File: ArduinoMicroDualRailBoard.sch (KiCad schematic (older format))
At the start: 54 parts, among them J1 Conn_01x20_Male, J2 Screw_Terminal_01x03, J3 Conn_01x20_Male, J4 Conn_01x20_Male, J5 Screw_Terminal_01x03, J6 Conn_01x20_Male, J7 SDS-50J, J8 SDS-50J, U1 L7805, U2 L7815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

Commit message: PCB layout #2
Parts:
- added J9: Screw_Terminal_01x03, TerminalBlock:TerminalBlock_bornier-3_P5.08mm, symbol Connector:Screw_Terminal_01x03
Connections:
- net +15V: now also J9.3 (Pin_3)
- net -15V: now also J9.1 (Pin_1)
- net GND: now also J9.2 (Pin_2)
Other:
- moved on the sheet: J5
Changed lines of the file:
@@
 L Connector:Screw_Terminal_01x03 J5
 U 1 1 60BD4254
-P 3050 6100
-F 0 "J5" H 3000 5850 50  0000 L CNN
-F 1 "Screw_Terminal_01x03" V 3150 5700 50  0000 L CNN
-F 2 "TerminalBlock:TerminalBlock_bornier-3_P5.08mm" H 3050 6100 50  0001 C CNN
-F 3 "~" H 3050 6100 50  0001 C CNN
-	1    3050 6100
+P 3050 5750
+F 0 "J5" H 3000 5500 50  0000 L CNN
+F 1 "Screw_Terminal_01x03" V 3150 5350 50  0000 L CNN
+F 2 "TerminalBlock:TerminalBlock_bornier-3_P5.08mm" H 3050 5750 50  0001 C CNN
+F 3 "~" H 3050 5750 50  0001 C CNN
+	1    3050 5750
 	-1   0    0    1
 $EndComp
@@
 L power:+15V #PWR0131
 U 1 1 60C5B353
-P 3350 5900
-F 0 "#PWR0131" H 3350 5750 50  0001 C CNN
-F 1 "+15V" H 3365 6073 50  0000 C CNN
-F 2 "" H 3350 5900 50  0001 C CNN
-F 3 "" H 3350 5900 50  0001 C CNN
-	1    3350 5900
+P 3350 5550
+F 0 "#PWR0131" H 3350 5400 50  0001 C CNN
+F 1 "+15V" H 3365 5723 50  0000 C CNN
+F 2 "" H 3350 5550 50  0001 C CNN
+F 3 "" H 3350 5550 50  0001 C CNN
+	1    3350 5550
 	1    0    0    -1
 $EndComp
@@
 L power:GND #PWR0132
 U 1 1 60C5D4D3
-P 3550 6300
-F 0 "#PWR0132" H 3550 6050 50  0001 C CNN
-F 1 "GND" H 3555 6127 50  0000 C CNN
-F 2 "" H 3550 6300 50  0001 C CNN
-F 3 "" H 3550 6300 50  0001 C CNN
-	1    3550 6300
+P 3550 5950
+F 0 "#PWR0132" H 3550 5700 50  0001 C CNN
+F 1 "GND" H 3555 5777 50  0000 C CNN
+F 2 "" H 3550 5950 50  0001 C CNN
+F 3 "" H 3550 5950 50  0001 C CNN
+	1    3550 5950
 	1    0    0    -1
 $EndComp
@@
 L power:-15V #PWR0133
 U 1 1 60C5DC2B
-P 3350 6300
-F 0 "#PWR0133" H 3350 6400 50  0001 C CNN
-F 1 "-15V" H 3365 6473 50  0000 C CNN
-F 2 "" H 3350 6300 50  0001 C CNN
-F 3 "" H 3350 6300 50  0001 C CNN
-	1    3350 6300
-	-1   0    0    1
-$EndComp
-Wire Wire Line
-	3250 6200 3350 6200
-Wire Wire Line
-	3350 6200 3350 6300
-Wire Wire Line
-	3250 6100 3550 6100
-Wire Wire Line
-	3550 6100 3550 6300
-Wire Wire Line
-	3250 6000 3350 6000
-Wire Wire Line
-	3350 6000 3350 5900
+P 3350 5950
+F 0 "#PWR0133" H 3350 6050 50  0001 C CNN
+F 1 "-15V" H 3365 6123 50  0000 C CNN
+F 2 "" H 3350 5950 50  0001 C CNN
+F 3 "" H 3350 5950 50  0001 C CNN
+	1    3350 5950
+	-1   0    0    1
+$EndComp
+Wire Wire Line
+	3250 5850 3350 5850
+Wire Wire Line
+	3350 5850 3350 5950
+Wire Wire Line
+	3250 5750 3550 5750
+Wire Wire Line
+	3550 5750 3550 5950
+Wire Wire Line
+	3250 5650 3350 5650
+Wire Wire Line
+	3350 5650 3350 5550
 NoConn ~ 4200 5800
 NoConn ~ 6750 6400
@@
 Wire Wire Line
 	4100 4300 4200 4300
+$Comp
+L Connector:Screw_Terminal_01x03 J9
+U 1 1 5FC225DB
+P 3050 6700
+F 0 "J9" H 3000 6450 50  0000 L CNN
+F 1 "Screw_Terminal_01x03" V 3150 6300 50  0000 L CNN
+F 2 "TerminalBlock:TerminalBlock_bornier-3_P5.08mm" H 3050 6700 50  0001 C CNN
+F 3 "~" H 3050 6700 50  0001 C CNN
+	1    3050 6700
+	-1   0    0    1
+$EndComp
+$Comp
+L power:+15V #PWR01
+U 1 1 5FC225E1
+P 3350 6500
+F 0 "#PWR01" H 3350 6350 50  0001 C CNN
+F 1 "+15V" H 3365 6673 50  0000 C CNN
+F 2 "" H 3350 6500 50  0001 C CNN
+F 3 "" H 3350 6500 50  0001 C CNN
+	1    3350 6500
+	1    0    0    -1
+$EndComp
+$Comp
+L power:GND #PWR03
+U 1 1 5FC225E7
+P 3550 6900
+F 0 "#PWR03" H 3550 6650 50  0001 C CNN
+F 1 "GND" H 3555 6727 50  0000 C CNN
+F 2 "" H 3550 6900 50  0001 C CNN
+F 3 "" H 3550 6900 50  0001 C CNN
+	1    3550 6900
+	1    0    0    -1
+$EndComp
+$Comp
+L power:-15V #PWR02
+U 1 1 5FC225ED
+P 3350 6900
+F 0 "#PWR02" H 3350 7000 50  0001 C CNN
+F 1 "-15V" H 3365 7073 50  0000 C CNN
+F 2 "" H 3350 6900 50  0001 C CNN
+F 3 "" H 3350 6900 50  0001 C CNN
+	1    3350 6900
+	-1   0    0    1
+$EndComp
+Wire Wire Line
+	3250 6800 3350 6800
+Wire Wire Line
+	3350 6800 3350 6900
+Wire Wire Line
+	3250 6700 3550 6700
+Wire Wire Line
+	3550 6700 3550 6900
+Wire Wire Line
+	3250 6600 3350 6600
+Wire Wire Line
+	3350 6600 3350 6500
 $EndSCHEMATC

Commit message: Finished routing
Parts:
- added J10: Conn_01x02_Male, Connector_PinHeader_2.54mm:PinHeader_1x02_P2.54mm_Vertical, symbol Connector:Conn_01x02_Male
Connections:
- net +5V: now also J10.2 (Pin_2); no longer C14.2, U4.12 (+5V)
- new net: C14.2, J10.1 (Pin_1), U4.12 (+5V)
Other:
- note added: "PLACE JUMPER FOR NORMAL OPERATION\nREMOVE JUMPER WHEN POWERED BY USB"
- note added: "V"
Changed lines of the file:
@@
 L power:+5V #PWR0112
 U 1 1 5FE7786C
-P 6750 6050
-F 0 "#PWR0112" H 6750 5900 50  0001 C CNN
-F 1 "+5V" H 6765 6223 50  0000 C CNN
-F 2 "" H 6750 6050 50  0001 C CNN
-F 3 "" H 6750 6050 50  0001 C CNN
-	1    6750 6050
+P 7100 5500
+F 0 "#PWR0112" H 7100 5350 50  0001 C CNN
+F 1 "+5V" H 7115 5673 50  0000 C CNN
+F 2 "" H 7100 5500 50  0001 C CNN
+F 3 "" H 7100 5500 50  0001 C CNN
+	1    7100 5500
 	1    0    0    -1
 $EndComp
@@
 Wire Wire Line
 	6500 6100 6750 6100
-Wire Wire Line
-	6750 6100 6750 6050
 $Comp
 L Device:C C14
@@
 Wire Wire Line
 	3350 6600 3350 6500
+$Comp
+L Connector:Conn_01x02_Male J10
+U 1 1 5FD0AFC4
+P 7400 5700
+F 0 "J10" H 7372 5582 50  0000 R CNN
+F 1 "Conn_01x02_Male" H 7850 5750 50  0000 R CNN
+F 2 "Connector_PinHeader_2.54mm:PinHeader_1x02_P2.54mm_Vertical" H 7400 5700 50  0001 C CNN
+F 3 "~" H 7400 5700 50  0001 C CNN
+	1    7400 5700
+	-1   0    0    1
+$EndComp
+Wire Wire Line
+	6750 5700 7200 5700
+Wire Wire Line
+	6750 5700 6750 6100
+Wire Wire Line
+	7100 5500 7100 5600
+Wire Wire Line
+	7100 5600 7200 5600
+Text Notes 5950 5200 0    50   ~ 0
+PLACE JUMPER FOR NORMAL OPERATION\nREMOVE JUMPER WHEN POWERED BY USB
+Wire Notes Line
+	7350 5500 7350 5250
+Text Notes 7396 5549 2    100  ~ 0
+V
 $EndSCHEMATC

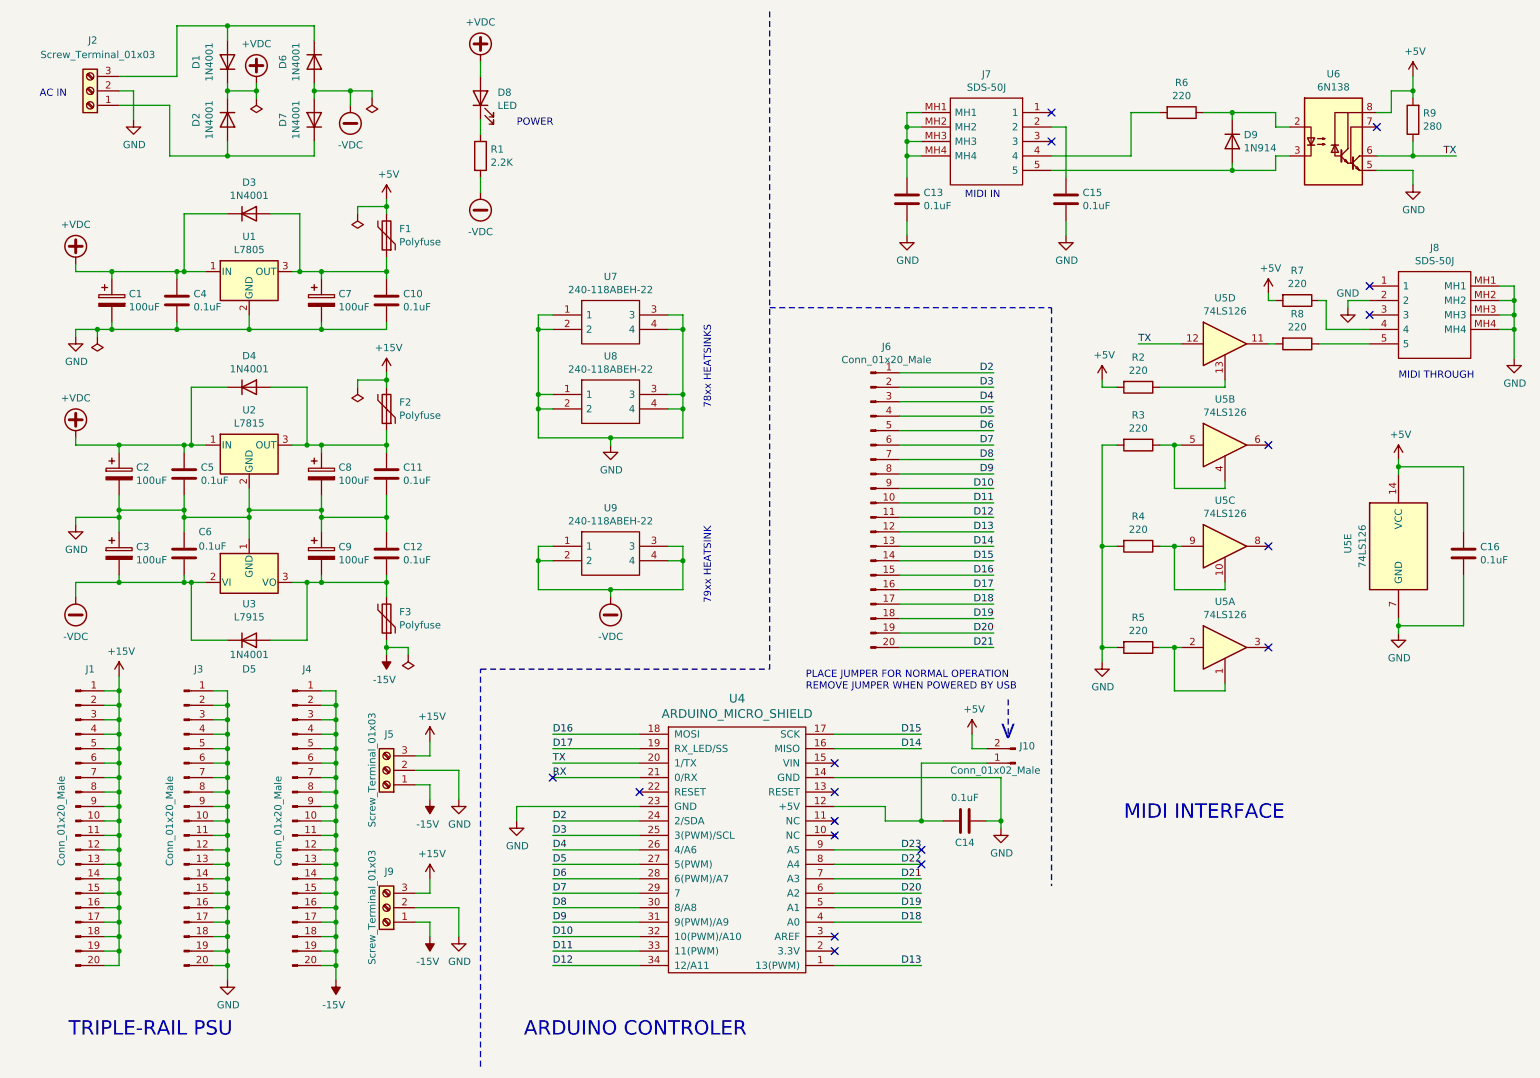
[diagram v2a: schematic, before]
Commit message: Updated Gerbers, fixed RX/TX reversal on Arduino
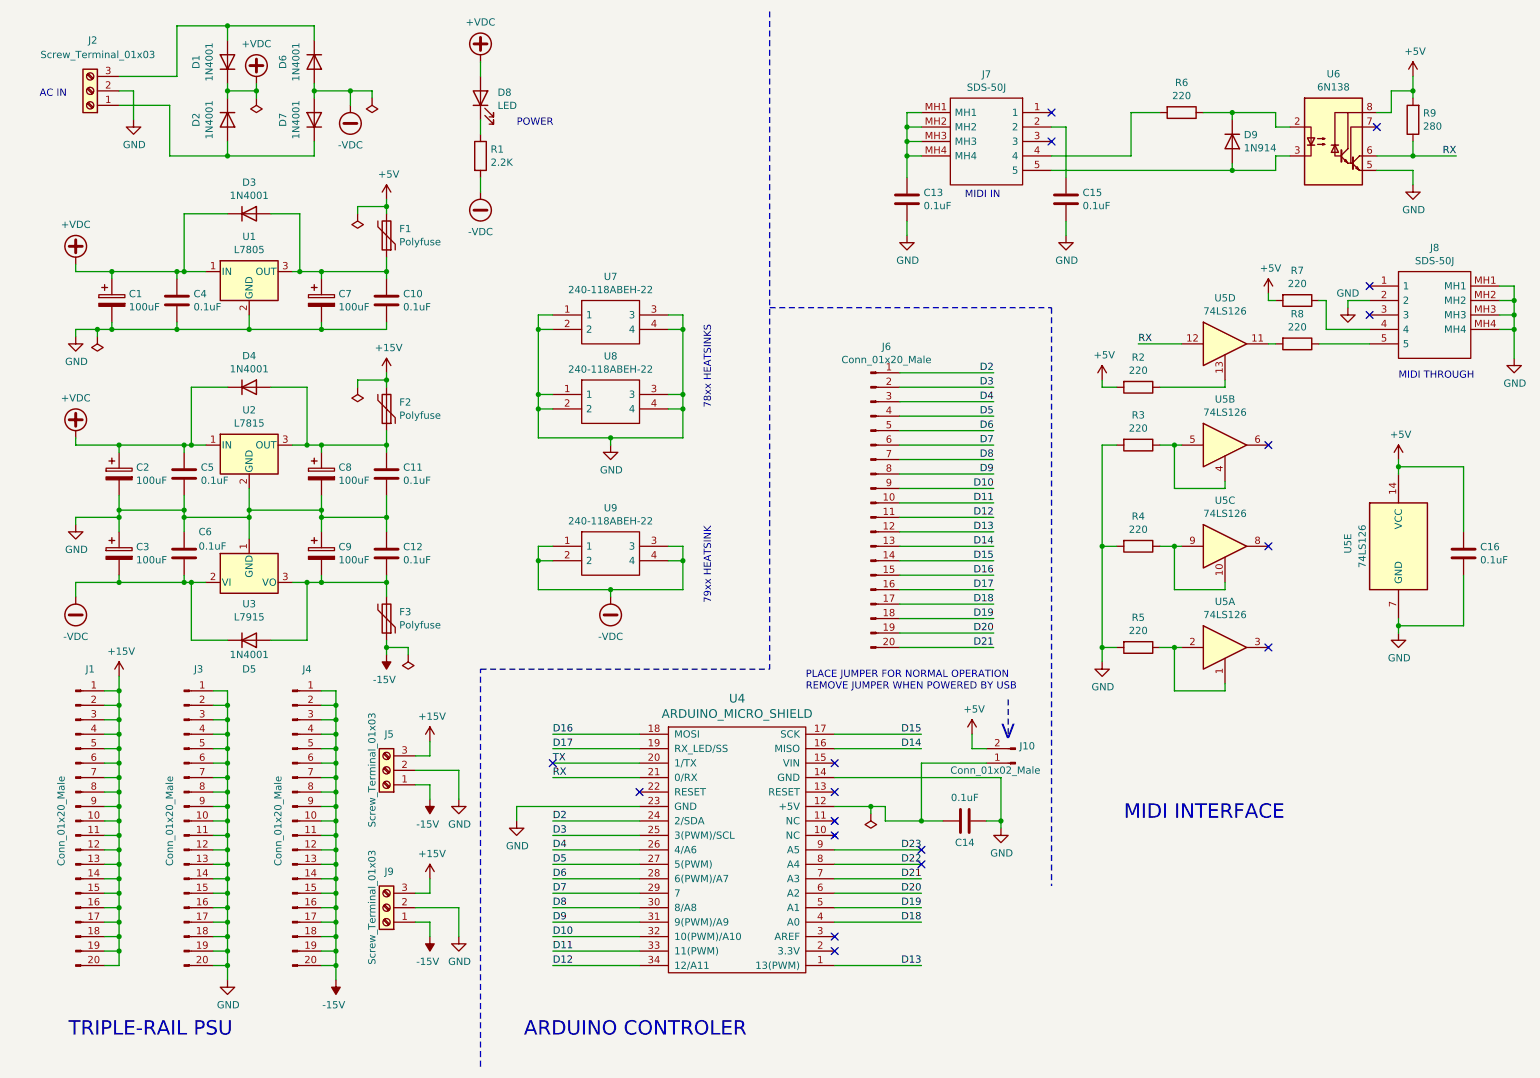
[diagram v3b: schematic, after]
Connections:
- net RX: now also R9.1, U5.12, U6.6 (VO2)
- net TX: no longer R9.1, U5.12, U6.6 (VO2)
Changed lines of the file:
@@
 $EndComp
 Wire Wire Line
-	6150 6000 6500 6000
+	6150 6000 6400 6000
 Wire Wire Line
 	6500 6000 6500 6100
@@
 	9900 1600 10150 1600
 Text Label 10450 1500 2    50   ~ 0
-TX
+RX
 $Comp
 L SamacSys_Parts:SDS-50J J8
@@
 $EndComp
 Text Label 8250 2800 0    50   ~ 0
-TX
+RX
 Wire Wire Line
 	8250 2800 8550 2800
@@
 Wire Wire Line
 	3350 5650 3350 5550
-NoConn ~ 4200 5800
+NoConn ~ 4200 5700
 NoConn ~ 6750 6400
 NoConn ~ 6750 6300
@@
 Text Notes 7396 5549 2    100  ~ 0
 V
+$Comp
+L power:PWR_FLAG #FLG0107
+U 1 1 5FC35D0A
+P 6400 6050
+F 0 "#FLG0107" H 6400 6125 50  0001 C CNN
+F 1 "PWR_FLAG" H 6400 6223 50  0001 C CNN
+F 2 "" H 6400 6050 50  0001 C CNN
+F 3 "~" H 6400 6050 50  0001 C CNN
+	1    6400 6050
+	-1   0    0    1
+$EndComp
+Wire Wire Line
+	6400 6000 6400 6050
+Connection ~ 6400 6000
+Wire Wire Line
+	6400 6000 6500 6000
 $EndSCHEMATC
